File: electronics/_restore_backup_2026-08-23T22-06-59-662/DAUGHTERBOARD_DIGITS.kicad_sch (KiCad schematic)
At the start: 19 parts, among them J11 MEZ_SIGNALS, J12 MEZ_SIGNALS, Q2 AO3400A, Q3 AO3400A, U4 GS2022CW-G, U5 74HC157, U6 HEF4543B, U7 74LVC1GU04DRL, U8 74HC595, U9 74LVC1GU04DRL

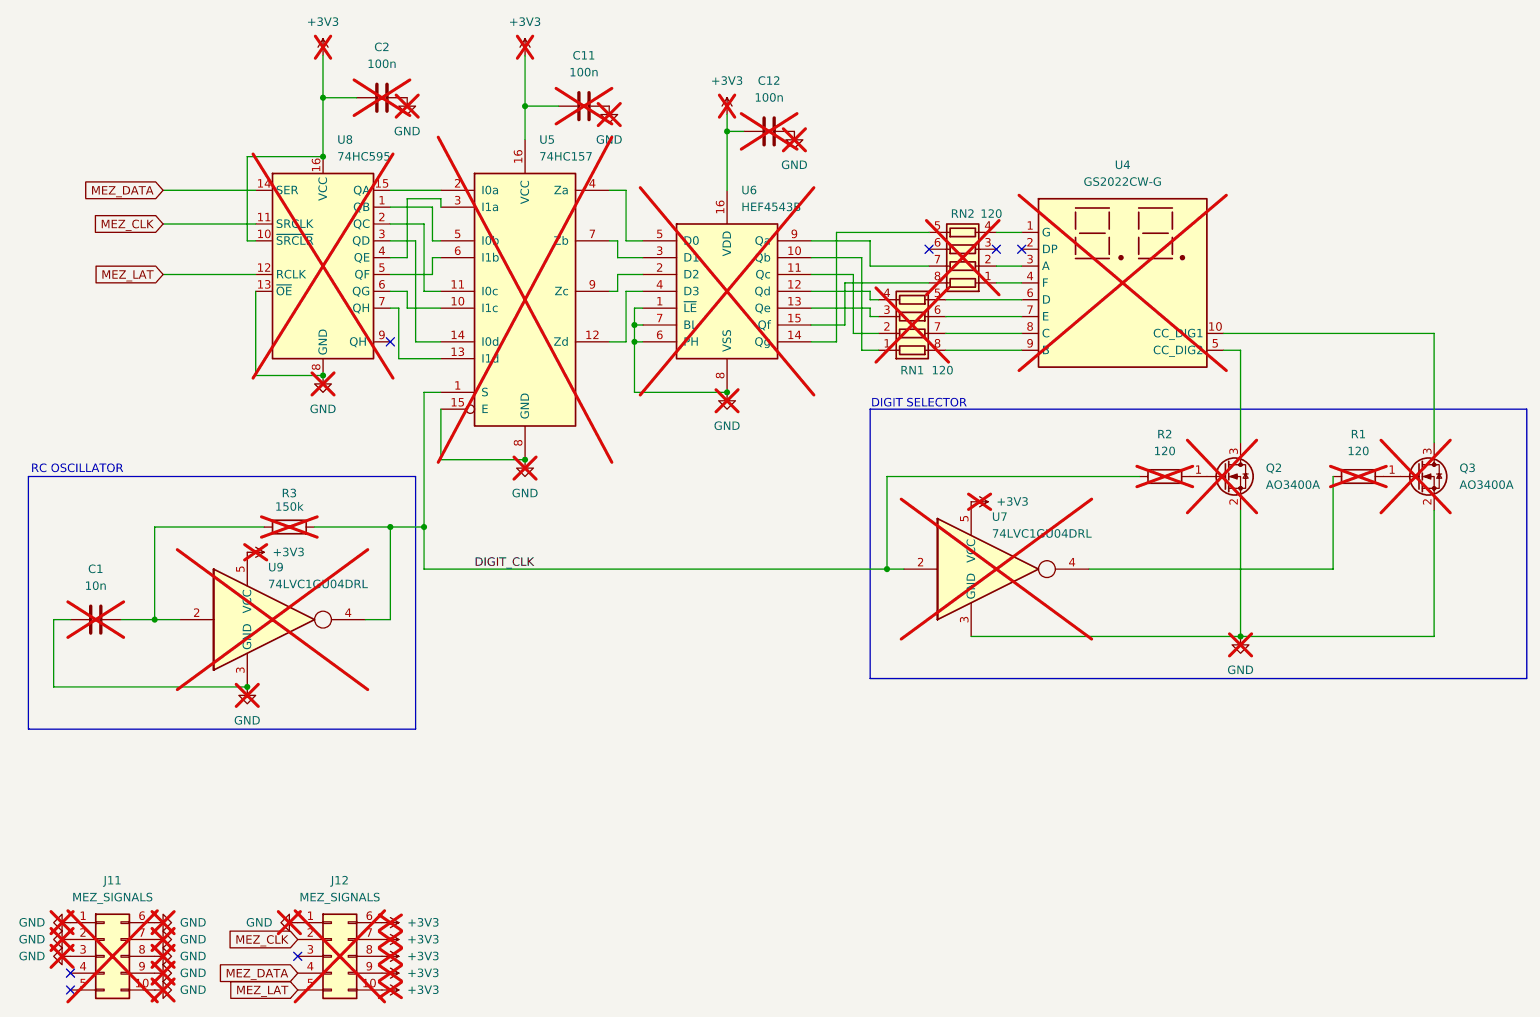
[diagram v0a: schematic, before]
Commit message: Add new 2S powerstage
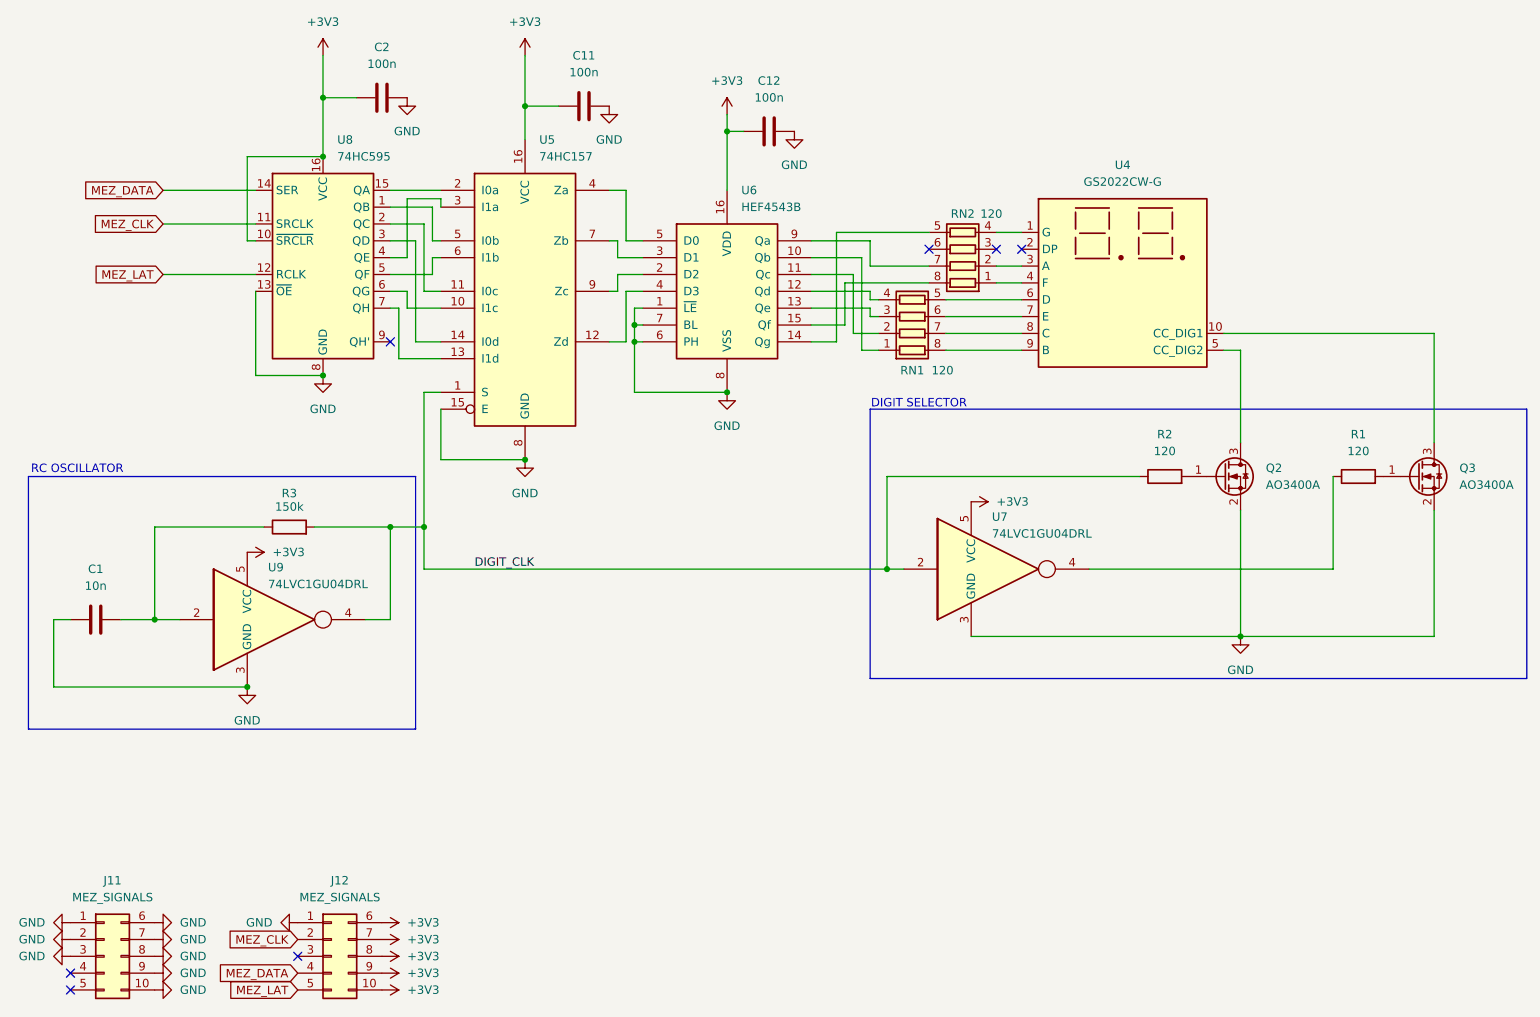
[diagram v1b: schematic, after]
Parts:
- C1, C11, C12, C2, J11, J12, Q2, Q3, R1, R2, R3, RN1, RN2, U4, U5, U6, U7, U8, U9: now fitted; now in the parts list
